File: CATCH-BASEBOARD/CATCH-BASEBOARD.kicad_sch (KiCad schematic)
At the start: 4 parts, among them J1 SJ3-35083B-TR, U1 PC817

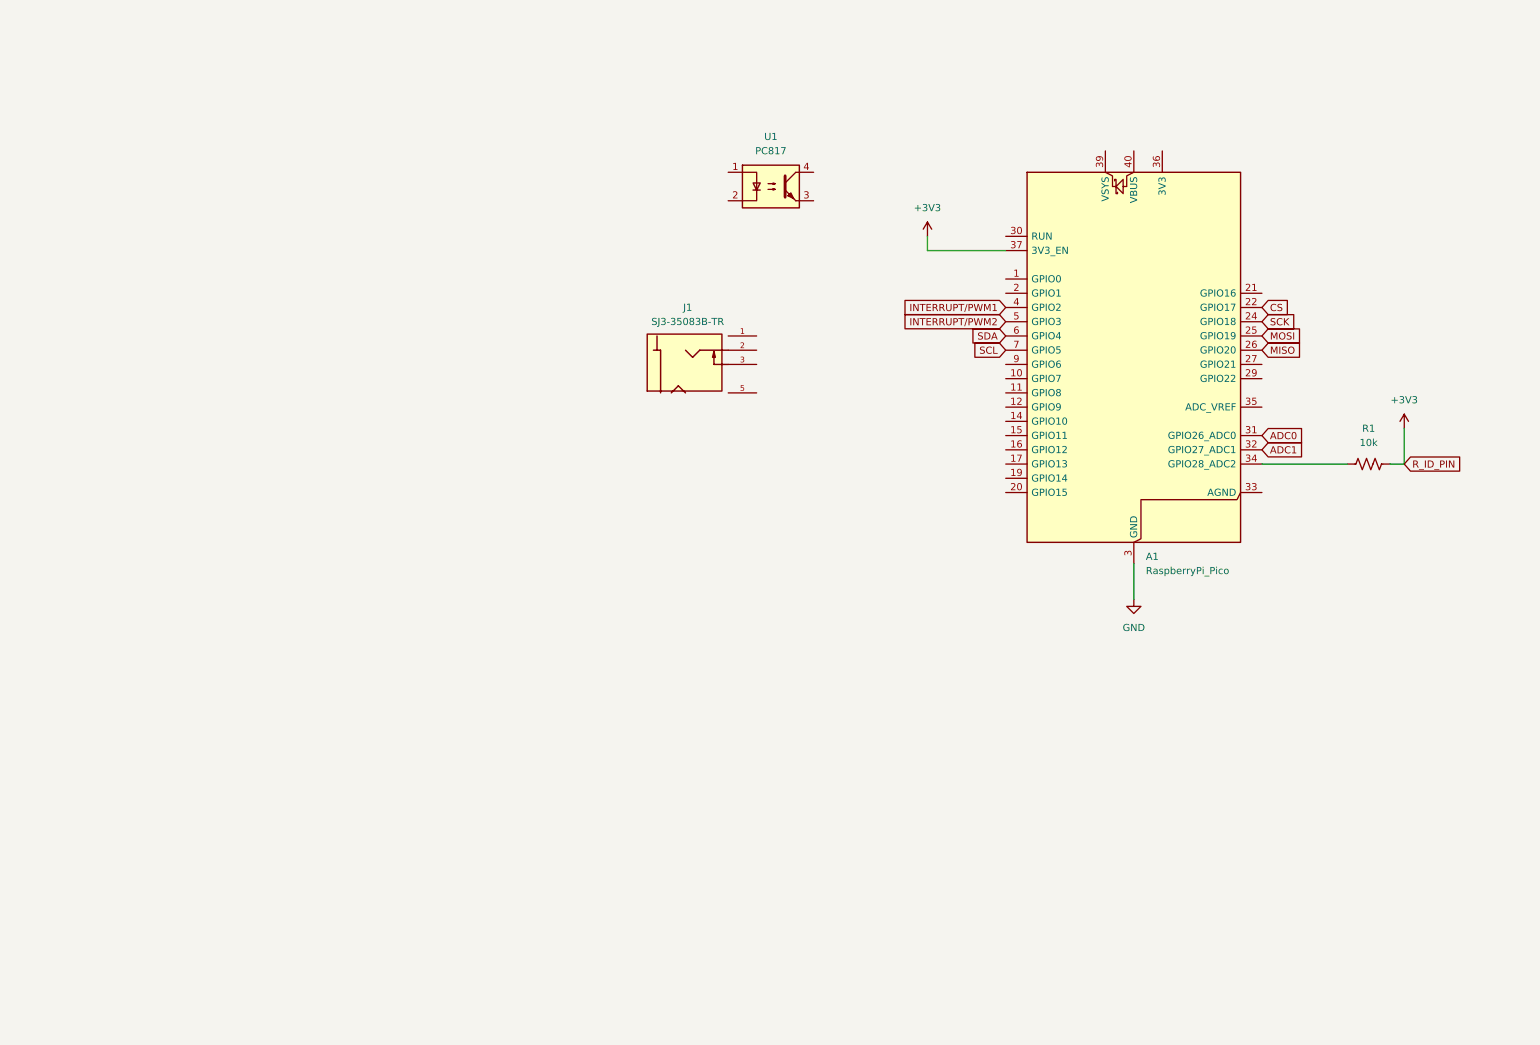
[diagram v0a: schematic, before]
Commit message: ADDITIONS TO SCHEMATIC
Fleshed out schematic more, added load switch and connectors. Imported new models. Need to work on battery logistics then start PCB.
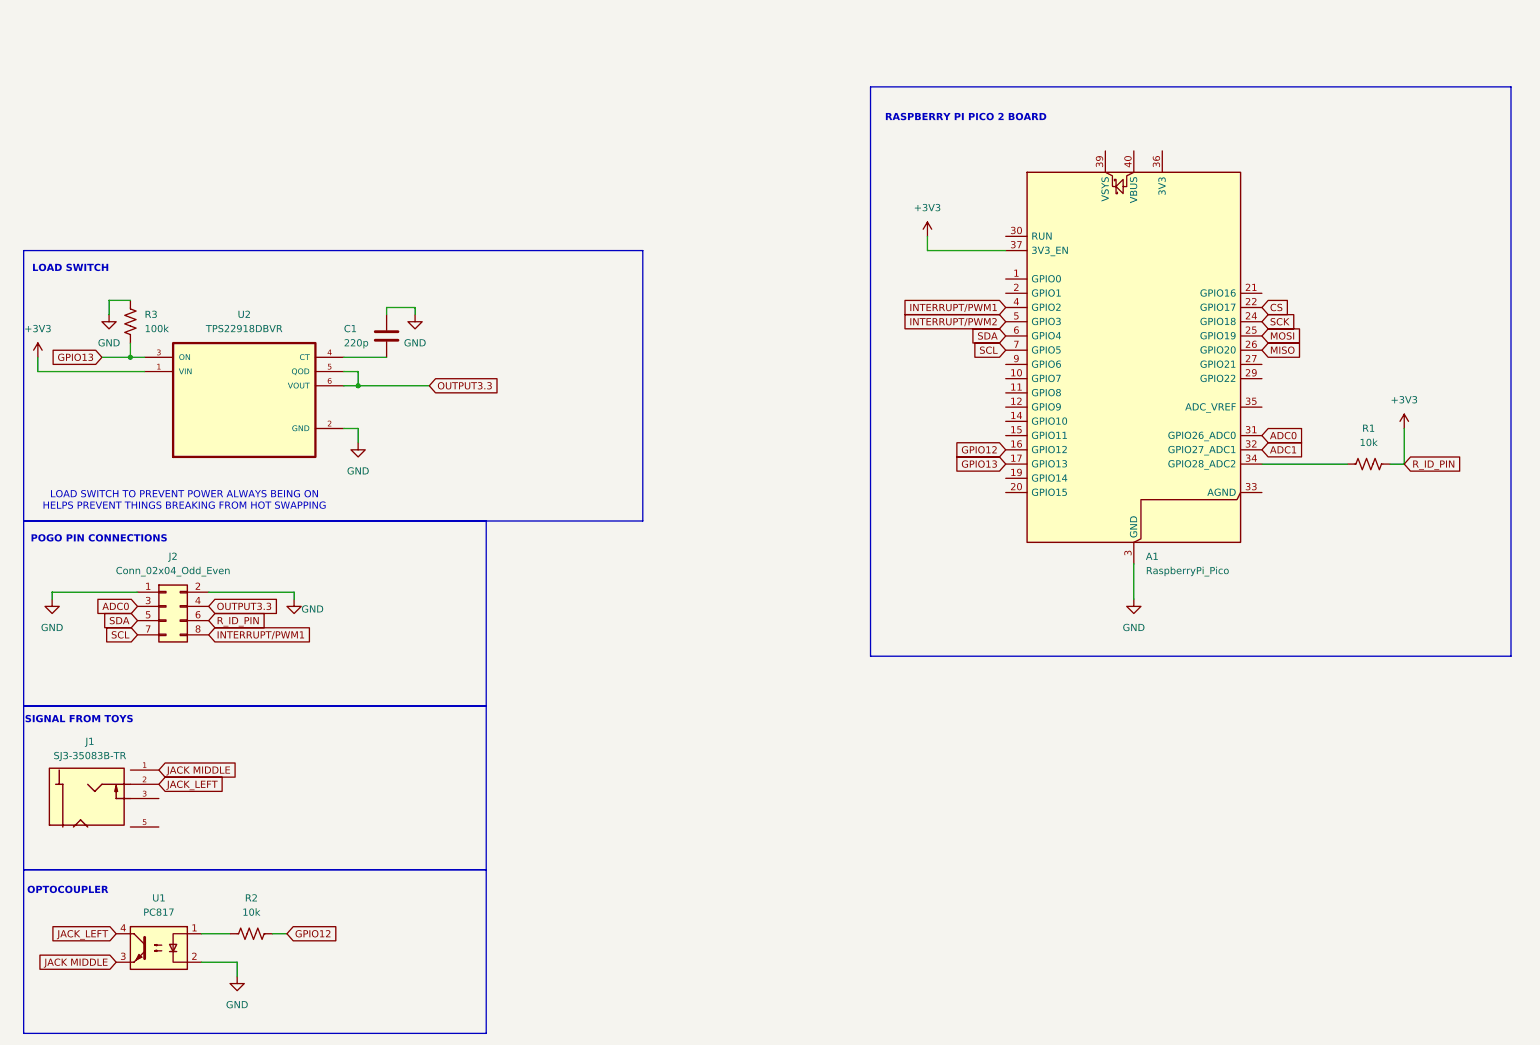
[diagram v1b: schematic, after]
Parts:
- added C1: 220p, symbol Device:C
- added J2: Conn_02x04_Odd_Even, symbol Connector_Generic:Conn_02x04_Odd_Even
- added R2: 10k, symbol Device:R_US
- added R3: 100k, symbol Device:R_US
- added U2: TPS22918DBVR, TPS22918DBVR:SOT95P280X145-6N, symbol TPS22918DBVR:TPS22918DBVR
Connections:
- net +3V3: now also J2.6 (Pin_6), U2.1 (VIN)
- net ADC0: now also J2.3 (Pin_3)
- net GND: now also U1.2, C1.1, J2.1 (Pin_1), J2.2 (Pin_2), R3.1, U2.2 (GND)
- net INTERRUPT/PWM1: now also J2.8 (Pin_8)
- net SCL: now also J2.7 (Pin_7)
- net SDA: now also J2.5 (Pin_5)
- net at U1.1: now also R2.1
- net JACK MIDDLE: now reaches U1.3
- net JACK MIDDLE: now also J1.1
- net JACK_LEFT: now reaches U1.4
- net JACK_LEFT: now also J1.2
- net GPIO12: now reaches A1.16 (GPIO12)
- net GPIO12: now also R2.2
- net GPIO13: now reaches A1.17 (GPIO13)
- net GPIO13: now also R3.2, U2.3 (ON)
- new net: C1.2, U2.4 (CT)
- new net OUTPUT3.3: J2.4 (Pin_4), U2.5 (QOD), U2.6 (VOUT)
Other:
- note added: "LOAD SWITCH"
- note added: "LOAD SWITCH TO PREVENT POWER ALWAYS BEING ON HELPS PREVENT THINGS BREAKING FROM HOT SWAPPING"
- note added: "OPTOCOUPLER"
- note added: "POGO PIN CONNECTIONS"
- note added: "RASPBERRY PI PICO 2 BOARD"
- note added: "SIGNAL FROM TOYS"
- moved on the sheet: J1, U1

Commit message: Fleshed Out Battery System
Added safeties to the battery system, reducing potential harm when programming. Added parts, and updated schematic.
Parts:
- added C2: 1u, symbol Device:C
- added JP1: SolderJumper_2_Open, symbol Jumper:SolderJumper_2_Open
- added R4: 100k, symbol Device:R_US
- added SW1: SW_SPST, symbol Switch:SW_SPST
- added U3: DMG2305UX-13, SOT-23_DIO, symbol DMG2305UX:DMG2305UX-13
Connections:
- net +3V3: now also A1.36 (3V3), C2.1; no longer A1.37 (3V3_EN)
- net VSYS: now reaches A1.39 (VSYS)
- net VSYS: now also JP1.1 (A), U3.3 (D)
- net VUSB: now reaches A1.40 (VBUS)
- net VUSB: now also R4.2, U3.1 (G)
- net GND renamed -BATT
- net -BATT: now also C2.2
- new net: JP1.2 (B), R4.1, SW1.2 (B), U3.2 (S)
- new net +BATT: SW1.1 (A)
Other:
- note added: "BATTERY CONNECTIONS + PMOSFET"
- note added: "PMOS used to protect batteries in case if the USB was connected at the same time Blocks the connection if the USB was plugged in. Solder jumper included in case if this doesnt work"
- note added: "Uses the PICO 2 breakout board, supposed to be soldered onto on the castellations. R_ID_PIN is used to identify the sensor that is interfacing with the board."

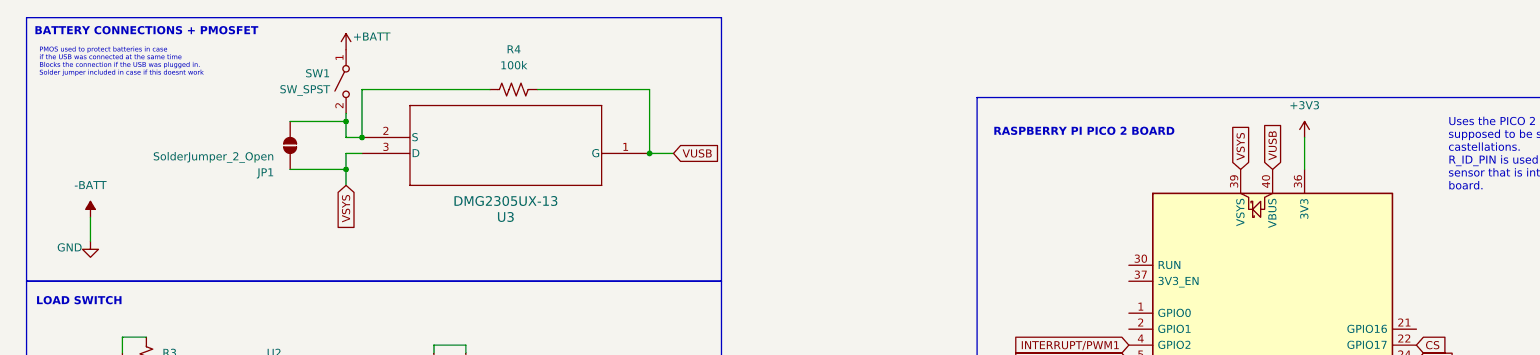
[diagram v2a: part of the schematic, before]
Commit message: Start of Layout
Added final parts in the schematic (battery connections, switches), assigned footprints, and started layout. Added rough size of PCB, placed some components.
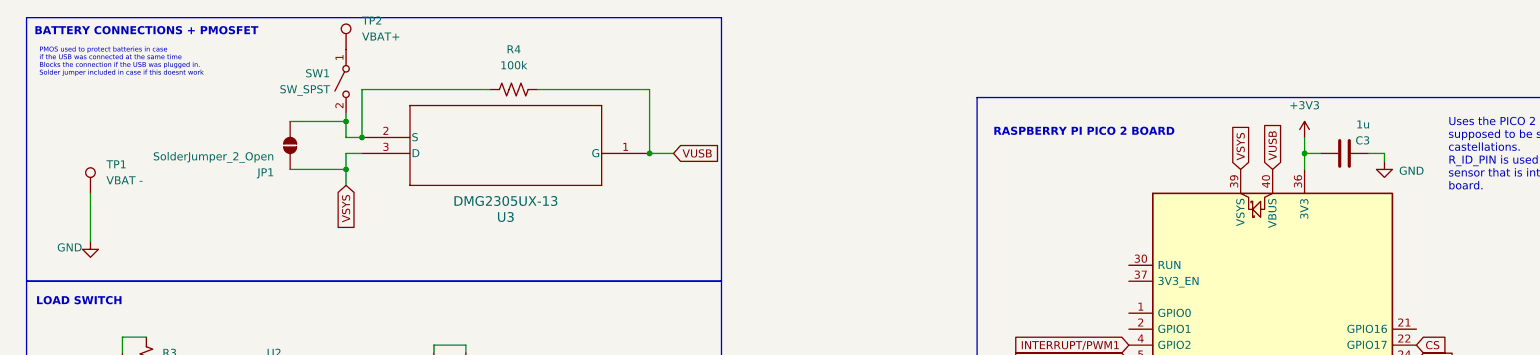
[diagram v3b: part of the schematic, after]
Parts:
- added C3: 1u, Capacitor_THT:C_Disc_D5.0mm_W2.5mm_P5.00mm, symbol Device:C
- added TP1: VBAT -, Connector_Wire:SolderWire-0.5sqmm_1x01_D0.9mm_OD2.1mm, symbol Connector:TestPoint
- added TP2: VBAT+, Connector_Wire:SolderWire-0.5sqmm_1x01_D0.9mm_OD2.1mm, symbol Connector:TestPoint
- C1, C2: footprint (none) -> Capacitor_THT:C_Disc_D5.0mm_W2.5mm_P5.00mm
- J1: footprint SJ3-35083B-TR:SAMESKY_SJ3-35083B-TR -> footprints:SAMESKY_SJ3-35083B-TR
- J2: footprint (none) -> POGOSTUFF:POGO_2x4_THT
- JP1: footprint (none) -> Jumper:SolderJumper-2_P1.3mm_Open_RoundedPad1.0x1.5mm
- R1, R2, R3, R4: footprint (none) -> Resistor_THT:R_Axial_DIN0207_L6.3mm_D2.5mm_P7.62mm_Horizontal
- SW1: footprint (none) -> Connector_Wire:SolderWire-0.5sqmm_1x02_P4.6mm_D0.9mm_OD2.1mm
- U2: footprint TPS22918DBVR:SOT95P280X145-6N -> footprints:SOT95P280X145-6N
- U3: footprint SOT-23_DIO -> footprints:DMG2305UX
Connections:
- net +3V3: now also C3.1
- net +BATT: no longer names the net of SW1.1 (A)
- net +BATT: now also TP2.1
- net -BATT renamed GND
- net GND: now also C3.2, TP1.1

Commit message: First Layout Revision
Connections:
- net GND: now also U1.3; no longer U1.2
- net JACK MIDDLE: now also U1.2; no longer U1.3
- net JACK_LEFT: now also U1.1; no longer U1.4
- net SCL: now also J2.5 (Pin_5); no longer J2.7 (Pin_7)
- net SDA: now also J2.7 (Pin_7); no longer J2.5 (Pin_5)
- net at R2.1: now also U1.4; no longer U1.1

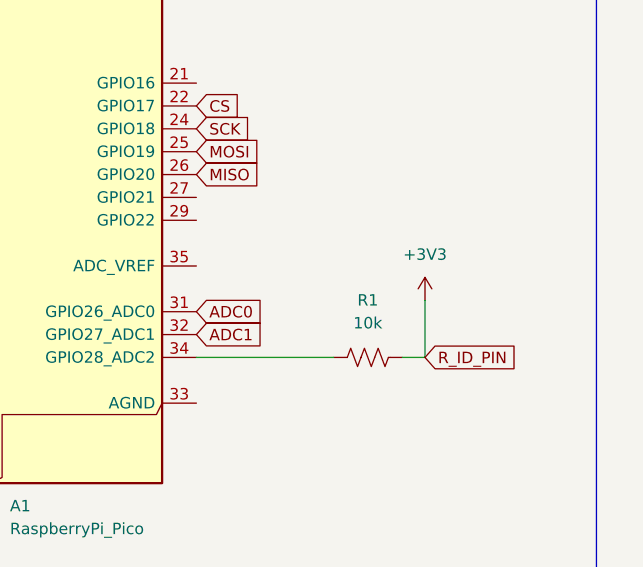
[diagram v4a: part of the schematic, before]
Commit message: Fixed Schematic + Finished Layout v.1
Layout still needs some touching up on, especially vias. I'll be changing it to fix all the errors on the DRC.
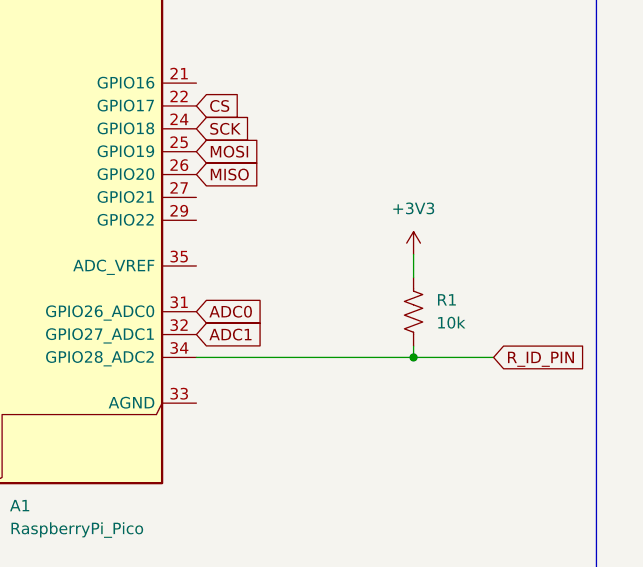
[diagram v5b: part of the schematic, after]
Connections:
- net +3V3: no longer J2.6 (Pin_6)
- net R_ID_PIN: now reaches A1.34 (GPIO28_ADC2), R1.1
- net R_ID_PIN: now also J2.6 (Pin_6)
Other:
- moved on the sheet: R1
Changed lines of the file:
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@@
+	)
+	(junction
+		(at 264.16 92.71)
+		(diameter 0)
+		(color 0 0 0 0)
 	)
 	(junction
@@
 	(wire
 		(pts
-			(xy 265.43 86.36) (xy 265.43 92.71)
-		)
-		(stroke
-			(width 0)
-			(type default)
-		)
-	)
-	(wire
-		(pts
 			(xy 217.17 110.49) (xy 217.17 116.84)
 		)
@@
 	(wire
 		(pts
+			(xy 264.16 81.28) (xy 264.16 83.82)
+		)
+		(stroke
+			(width 0)
+			(type default)
+		)
+	)
+	(wire
+		(pts
 			(xy 21.59 73.66) (xy 21.59 76.2)
 		)
@@
 	(wire
 		(pts
-			(xy 255.27 92.71) (xy 240.03 92.71)
+			(xy 240.03 92.71) (xy 264.16 92.71)
 		)
 		(stroke
@@
 	(wire
 		(pts
+			(xy 264.16 92.71) (xy 273.05 92.71)
+		)
+		(stroke
+			(width 0)
+			(type default)
+		)
+	)
+	(wire
+		(pts
 			(xy 34.29 63.5) (xy 38.1 63.5)
 		)
@@
 	(wire
 		(pts
-			(xy 265.43 92.71) (xy 262.89 92.71)
+			(xy 264.16 91.44) (xy 264.16 92.71)
 		)
 		(stroke
@@
 	(global_label "R_ID_PIN"
 		(shape input)
-		(at 265.43 92.71 0)
+		(at 273.05 92.71 0)
 		(fields_autoplaced yes)
 		(effects
@@
 		)
 		(property "Intersheetrefs" "${INTERSHEET_REFS}"
-			(at 276.7005 92.71 0)
+			(at 284.3205 92.71 0)
 			(effects
 				(font
@@
 	(symbol
 		(lib_id "Device:R_US")
-		(at 259.08 92.71 90)
+		(at 264.16 87.63 180)
 		(unit 1)
 		(exclude_from_sim no)
@@
 		(fields_autoplaced yes)
 		(property "Reference" "R1"
-			(at 259.08 86.36 90)
-			(effects
-				(font
-					(size 1.27 1.27)
-				)
+			(at 266.7 86.3599 0)
+			(effects
+				(font
+					(size 1.27 1.27)
+				)
+				(justify right)
 			)
 		)
 		(property "Value" "10k"
-			(at 259.08 88.9 90)
-			(effects
-				(font
-					(size 1.27 1.27)
-				)
+			(at 266.7 88.8999 0)
+			(effects
+				(font
+					(size 1.27 1.27)
+				)
+				(justify right)
 			)
 		)
 		(property "Footprint" "Resistor_THT:R_Axial_DIN0207_L6.3mm_D2.5mm_P7.62mm_Horizontal"
-			(at 259.334 91.694 90)
+			(at 263.144 87.376 90)
 			(effects
 				(font
@@
 		)
 		(property "Datasheet" "~"
-			(at 259.08 92.71 0)
+			(at 264.16 87.63 0)
 			(effects
 				(font
@@
 		)
 		(property "Description" "Resistor, US symbol"
-			(at 259.08 92.71 0)
+			(at 264.16 87.63 0)
 			(effects
 				(font
@@
 	(symbol
 		(lib_id "power:+3V3")
-		(at 265.43 86.36 0)
+		(at 264.16 81.28 0)
 		(unit 1)
 		(exclude_from_sim no)
@@
 		(fields_autoplaced yes)
 		(property "Reference" "#PWR03"
-			(at 265.43 90.17 0)
+			(at 264.16 85.09 0)
 			(effects
 				(font
@@
 		)
 		(property "Value" "+3V3"
-			(at 265.43 81.28 0)
+			(at 264.16 76.2 0)
 			(effects
 				(font
@@
 		)
 		(property "Footprint" ""
-			(at 265.43 86.36 0)
+			(at 264.16 81.28 0)
 			(effects
 				(font
@@
 		)
 		(property "Datasheet" ""
-			(at 265.43 86.36 0)
+			(at 264.16 81.28 0)
 			(effects
 				(font
@@
 		)
 		(property "Description" "Power symbol creates a global label with name \"+3V3\""
-			(at 265.43 86.36 0)
-			(effects
-				(font
+			(at 264.16 81.28 0)
+			(effects
+				(font
